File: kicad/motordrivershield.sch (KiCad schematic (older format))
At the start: 40 parts, among them CN1 ARDUINO_MKR, CN2 QWIIC, P1 CONN_01X03, P2 CONN_01X03, U1 PCA9685_TSSOP28, U2 ADS1015

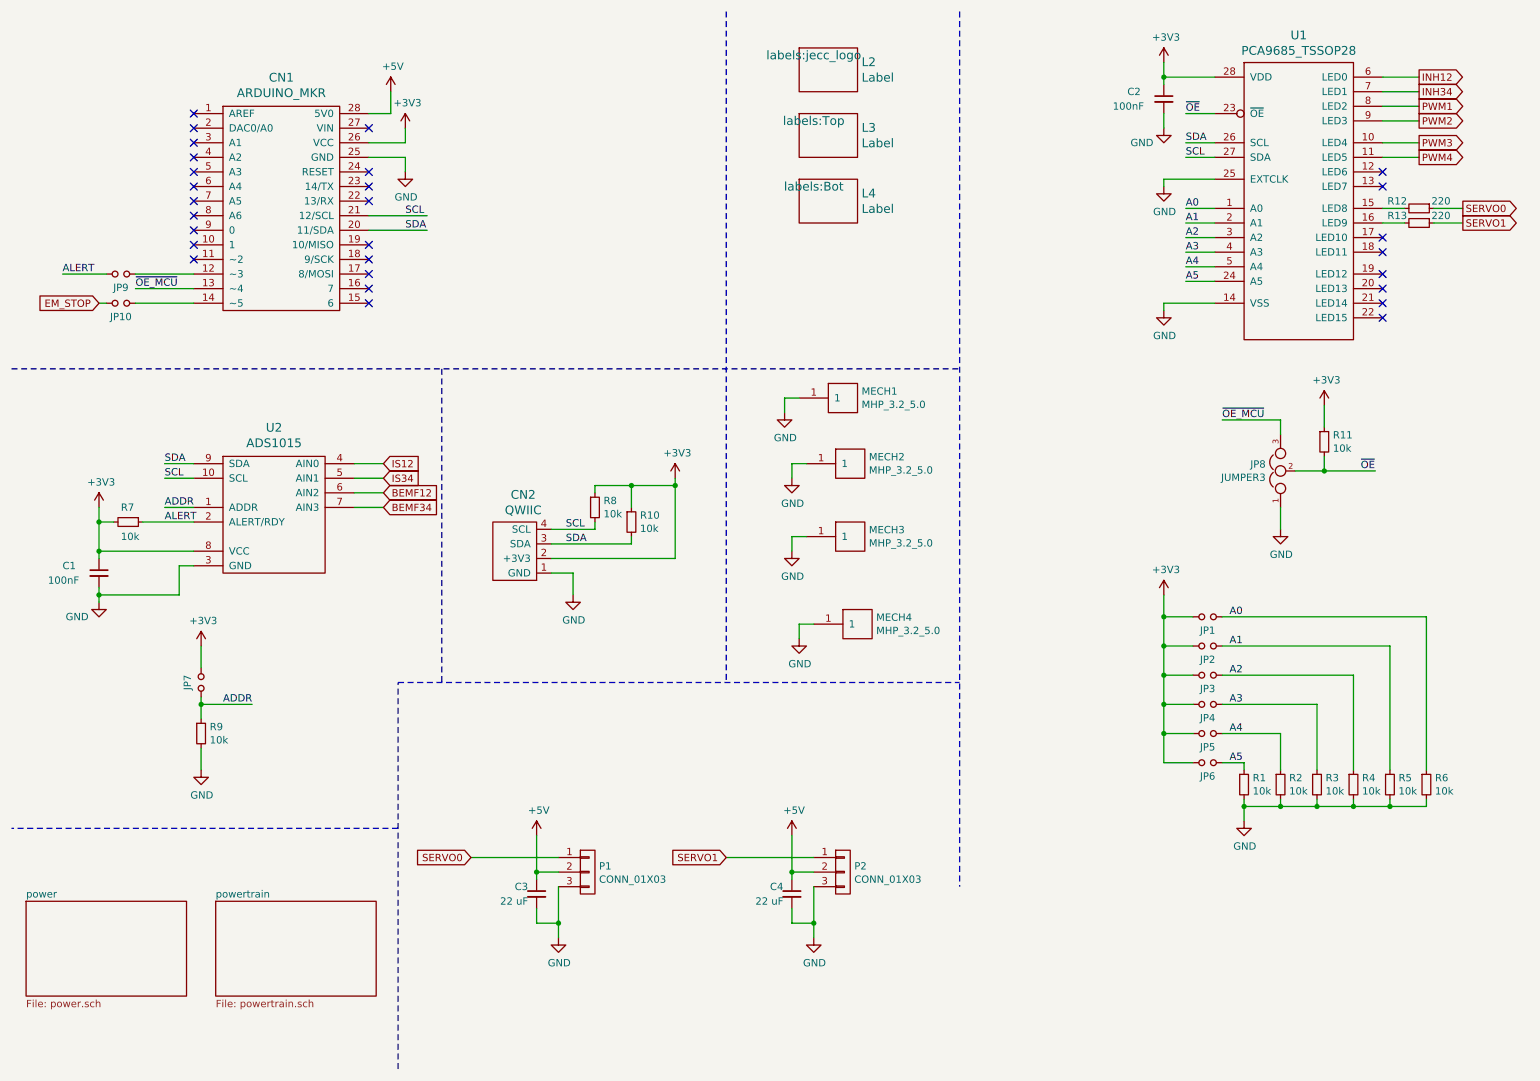
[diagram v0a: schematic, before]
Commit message: added nano footprint
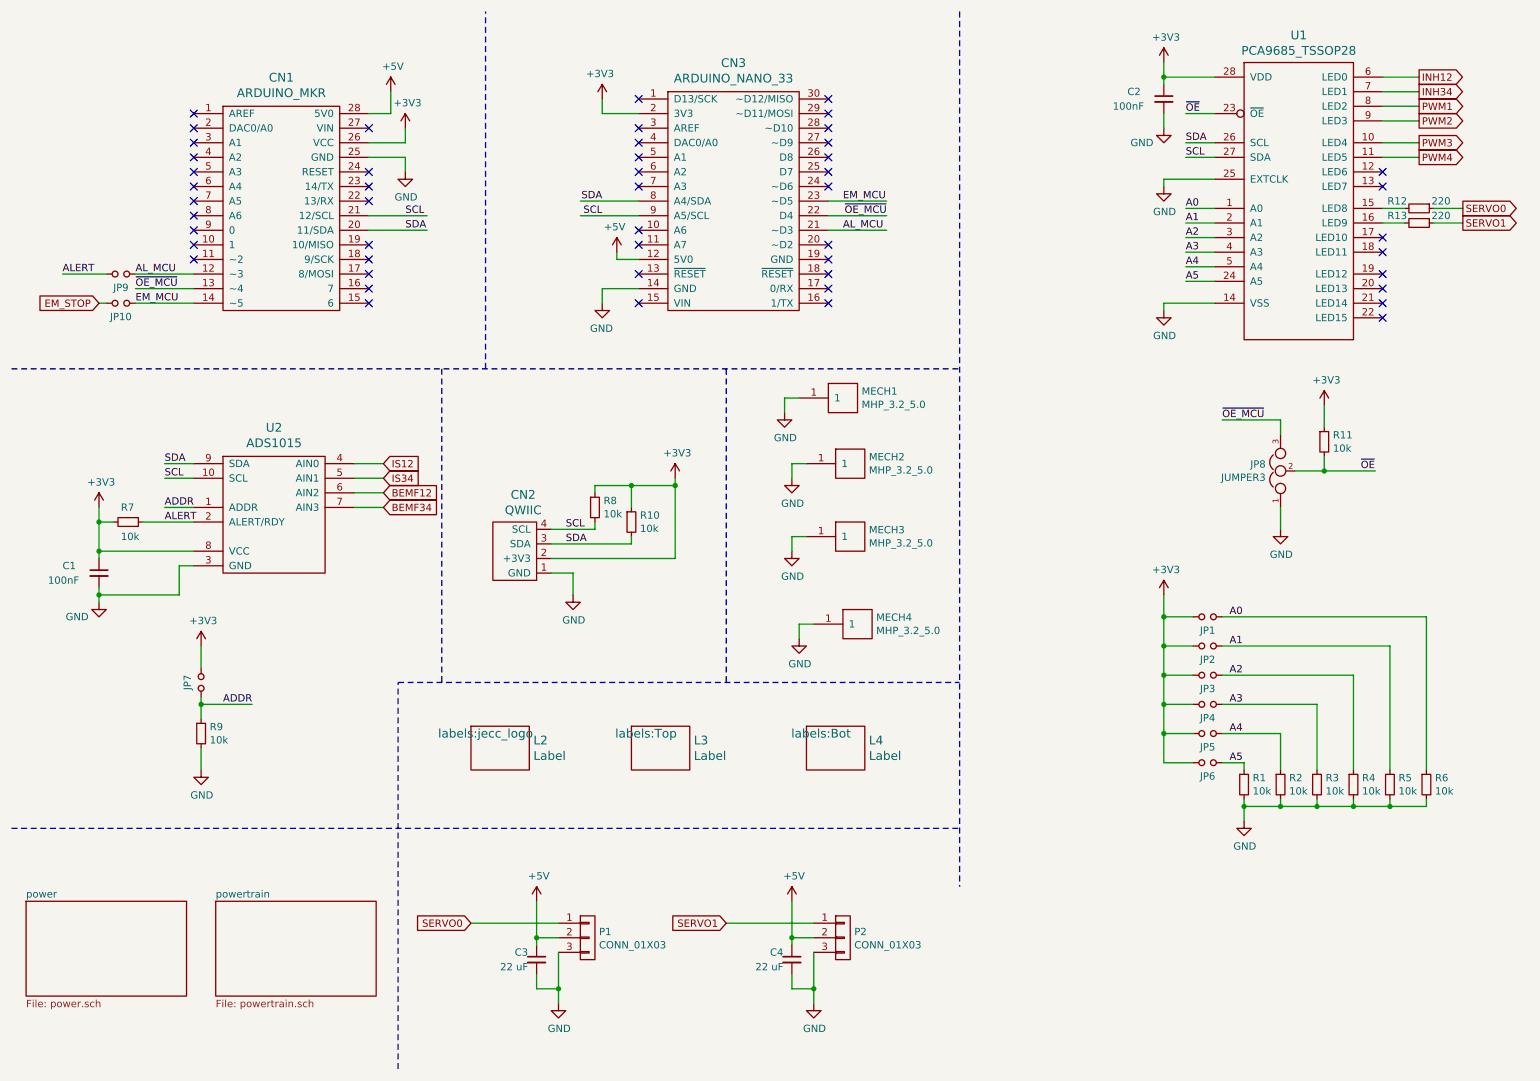
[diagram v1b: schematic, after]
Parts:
- added CN3: ARDUINO_NANO_33, MODULE_compute:ARDUINO_NANO_33, symbol MODULE_compute:ARDUINO_NANO_33
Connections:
- net labels added: AL_MCU, EM_MCU
- wire segments 143 -> 154
- no-connect marks 28 -> 50
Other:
- moved on the sheet: C3, C4, L2, L3, L4, P1, P2

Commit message: changed 5V power rail
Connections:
- wire segments 154 -> 156
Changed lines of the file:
@@
 NoConn ~ 2950 1700
 NoConn ~ 2950 1600
-NoConn ~ 2950 1300
 Wire Wire Line
 	4200 4350 4350 4350
@@
 	1150 2500 1100 2500
 Wire Wire Line
-	2950 1200 3100 1200
-Wire Wire Line
-	3100 1200 3100 1050
+	2950 1300 3100 1300
+Wire Wire Line
+	3100 1300 3100 1150
 $Comp
 L power-supply:+5V #PWR0115
 U 1 1 5F641F07
-P 3100 1050
-F 0 "#PWR0115" H 3100 900 50  0001 C CNN
-F 1 "+5V" H 3115 1223 50  0000 C CNN
-F 2 "" H 3100 1050 50  0000 C CNN
-F 3 "" H 3100 1050 50  0000 C CNN
-	1    3100 1050
+P 3100 1150
+F 0 "#PWR0115" H 3100 1000 50  0001 C CNN
+F 1 "+5V" H 3115 1323 50  0000 C CNN
+F 2 "" H 3100 1150 50  0000 C CNN
+F 3 "" H 3100 1150 50  0000 C CNN
+	1    3100 1150
 	1    0    0    -1
 $EndComp
@@
 Wire Notes Line
 	500  6100 7000 6100
-Wire Wire Line
-	4800 2200 4650 2200
-Wire Wire Line
-	4650 2200 4650 2150
-$Comp
-L power-supply:+5V #PWR0123
-U 1 1 5F68AA89
-P 4650 2150
-F 0 "#PWR0123" H 4650 2000 50  0001 C CNN
-F 1 "+5V" H 4665 2323 50  0000 C CNN
-F 2 "" H 4650 2150 50  0000 C CNN
-F 3 "" H 4650 2150 50  0000 C CNN
-	1    4650 2150
-	-1   0    0    -1
-$EndComp
 Wire Wire Line
 	4800 1200 4550 1200
@@
 	-1   0    0    -1
 $EndComp
-Wire Wire Line
-	4800 2400 4550 2400
 Wire Wire Line
 	4550 2400 4550 2500
@@
 NoConn ~ 6100 2400
 NoConn ~ 6100 2500
-NoConn ~ 4800 2500
 NoConn ~ 4800 2300
 NoConn ~ 4800 2100
@@
 Wire Notes Line
 	3750 2950 3750 500
+Wire Wire Line
+	4800 2400 4550 2400
+$Comp
+L power-supply:+5V #PWR0123
+U 1 1 5F68AA89
+P 4350 2400
+F 0 "#PWR0123" H 4350 2250 50  0001 C CNN
+F 1 "+5V" H 4365 2573 50  0000 C CNN
+F 2 "" H 4350 2400 50  0000 C CNN
+F 3 "" H 4350 2400 50  0000 C CNN
+	1    4350 2400
+	-1   0    0    -1
+$EndComp
+Wire Wire Line
+	4600 2500 4600 2450
+Wire Wire Line
+	4600 2450 4350 2450
+Wire Wire Line
+	4350 2450 4350 2400
+Wire Wire Line
+	4600 2500 4800 2500
+NoConn ~ 2950 1200
+NoConn ~ 4800 2200
 $EndSCHEMATC

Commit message: added leds, updated capacitor values and changed silkscreen
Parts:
- added D5, D6, D7, D8: Led_Small, LEDs:LED_0603, symbol devices:Led_Small
- added R15, R56, R57, R58: 1k, resistors:R_0603, symbol devices:R_0603
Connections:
- wire segments 156 -> 172
- no-connect marks 50 -> 46
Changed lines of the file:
@@
 Wire Wire Line
 	9900 1500 10150 1500
-NoConn ~ 9900 2300
-NoConn ~ 9900 2400
 NoConn ~ 9900 2500
 NoConn ~ 9900 2600
@@
 Wire Notes Line
 	3150 5100 7000 5100
-NoConn ~ 9900 2150
-NoConn ~ 9900 2050
 Wire Wire Line
 	1750 2300 1350 2300
@@
 NoConn ~ 2950 1200
 NoConn ~ 4800 2200
+$Comp
+L devices:R_0603 R15
+U 1 1 5F72B532
+P 10150 2050
+F 0 "R15" V 10100 1900 50  0000 C CNN
+F 1 "1k" V 10100 2200 50  0000 C CNN
+F 2 "resistors:R_0603" H 10150 1900 50  0001 C CNN
+F 3 "" H 10150 2050 50  0000 C CNN
+	1    10150 2050
+	0    1    1    0
+$EndComp
+$Comp
+L devices:R_0603 R56
+U 1 1 5F732F5D
+P 10150 2150
+F 0 "R56" V 10100 2000 50  0000 C CNN
+F 1 "1k" V 10100 2300 50  0000 C CNN
+F 2 "resistors:R_0603" H 10150 2000 50  0001 C CNN
+F 3 "" H 10150 2150 50  0000 C CNN
+	1    10150 2150
+	0    1    1    0
+$EndComp
+$Comp
+L devices:R_0603 R57
+U 1 1 5F73A7B5
+P 10150 2300
+F 0 "R57" V 10100 2150 50  0000 C CNN
+F 1 "1k" V 10100 2450 50  0000 C CNN
+F 2 "resistors:R_0603" H 10150 2150 50  0001 C CNN
+F 3 "" H 10150 2300 50  0000 C CNN
+	1    10150 2300
+	0    1    1    0
+$EndComp
+$Comp
+L devices:R_0603 R58
+U 1 1 5F742075
+P 10150 2400
+F 0 "R58" V 10100 2250 50  0000 C CNN
+F 1 "1k" V 10100 2550 50  0000 C CNN
+F 2 "resistors:R_0603" H 10150 2250 50  0001 C CNN
+F 3 "" H 10150 2400 50  0000 C CNN
+	1    10150 2400
+	0    1    1    0
+$EndComp
+$Comp
+L devices:Led_Small D5
+U 1 1 5F74A32D
+P 10550 2050
+F 0 "D5" H 10700 2000 50  0000 C CNN
+F 1 "Led_Small" H 10100 2000 50  0001 C CNN
+F 2 "LEDs:LED_0603" V 10550 2050 50  0001 C CNN
+F 3 "" V 10550 2050 50  0000 C CNN
+	1    10550 2050
+	-1   0    0    1
+$EndComp
+$Comp
+L devices:Led_Small D6
+U 1 1 5F74C44E
+P 10550 2150
+F 0 "D6" H 10700 2100 50  0000 C CNN
+F 1 "Led_Small" H 10100 2100 50  0001 C CNN
+F 2 "LEDs:LED_0603" V 10550 2150 50  0001 C CNN
+F 3 "" V 10550 2150 50  0000 C CNN
+	1    10550 2150
+	-1   0    0    1
+$EndComp
+$Comp
+L devices:Led_Small D7
+U 1 1 5F753DDF
+P 10550 2300
+F 0 "D7" H 10700 2250 50  0000 C CNN
+F 1 "Led_Small" H 10100 2250 50  0001 C CNN
+F 2 "LEDs:LED_0603" V 10550 2300 50  0001 C CNN
+F 3 "" V 10550 2300 50  0000 C CNN
+	1    10550 2300
+	-1   0    0    1
+$EndComp
+$Comp
+L devices:Led_Small D8
+U 1 1 5F75B602
+P 10550 2400
+F 0 "D8" H 10700 2350 50  0000 C CNN
+F 1 "Led_Small" H 10100 2350 50  0001 C CNN
+F 2 "LEDs:LED_0603" V 10550 2400 50  0001 C CNN
+F 3 "" V 10550 2400 50  0000 C CNN
+	1    10550 2400
+	-1   0    0    1
+$EndComp
+Wire Wire Line
+	9900 2050 10050 2050
+Wire Wire Line
+	9900 2150 10050 2150
+Wire Wire Line
+	9900 2300 10050 2300
+Wire Wire Line
+	9900 2400 10050 2400
+Wire Wire Line
+	10250 2050 10450 2050
+Wire Wire Line
+	10250 2150 10450 2150
+Wire Wire Line
+	10250 2300 10450 2300
+Wire Wire Line
+	10250 2400 10450 2400
+Wire Wire Line
+	10650 2050 10800 2050
+Wire Wire Line
+	10800 2050 10800 2150
+Wire Wire Line
+	10650 2150 10800 2150
+Connection ~ 10800 2150
+Wire Wire Line
+	10800 2150 10800 2300
+Wire Wire Line
+	10650 2300 10800 2300
+Connection ~ 10800 2300
+Wire Wire Line
+	10800 2300 10800 2400
+Wire Wire Line
+	10650 2400 10800 2400
+Connection ~ 10800 2400
+Wire Wire Line
+	10800 2400 10800 2500
+$Comp
+L power-supply:GND #PWR0196
+U 1 1 5F7C6534
+P 10800 2500
+F 0 "#PWR0196" H 10800 2250 50  0001 C CNN
+F 1 "GND" H 10805 2327 50  0000 C CNN
+F 2 "" H 10800 2500 50  0000 C CNN
+F 3 "" H 10800 2500 50  0000 C CNN
+	1    10800 2500
+	1    0    0    -1
+$EndComp
 $EndSCHEMATC

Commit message: bom update
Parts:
- C3, C4: value 22 uF -> 22uF
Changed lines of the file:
@@
 P 4100 7000
 F 0 "C3" H 3950 7050 50  0000 L CNN
-F 1 "22 uF" H 3850 6950 50  0000 L CNN
+F 1 "22uF" H 3850 6950 50  0000 L CNN
 F 2 "capacitors:C_1206" H 4100 6850 50  0001 C CNN
 F 3 "" H 4100 7000 50  0000 C CNN
@@
 P 5850 7000
 F 0 "C4" H 5700 7050 50  0000 L CNN
-F 1 "22 uF" H 5600 6950 50  0000 L CNN
+F 1 "22uF" H 5600 6950 50  0000 L CNN
 F 2 "capacitors:C_1206" H 5850 6850 50  0001 C CNN
 F 3 "" H 5850 7000 50  0000 C CNN

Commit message: swapped sda and scl on pca9685
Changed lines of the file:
@@
 $EndDescr
-$Comp
-L LED-controllers:PCA9685_TSSOP28 U1
-U 1 1 5F5F3EC3
-P 8750 2750
-F 0 "U1" H 9325 4837 60  0000 C CNN
-F 1 "PCA9685_TSSOP28" H 9325 4731 60  0000 C CNN
-F 2 "SSOP:TSSOP-28_4.4x9.7mm_Pitch0.65mm" H 9800 2600 60  0001 C CNN
-F 3 "" H 9350 2700 60  0000 C CNN
-	1    8750 2750
-	1    0    0    -1
-$EndComp
 $Comp
 L devices:Jumper_NO_Small JP1
@@
 	8550 1200 8750 1200
 Wire Wire Line
+	8750 1500 8550 1500
+Wire Wire Line
 	8750 1400 8550 1400
-Wire Wire Line
-	8750 1500 8550 1500
 Text Label 8550 1200 0    50   ~ 0
 ~OE
+Text Label 8550 1500 0    50   ~ 0
+SDA
 Text Label 8550 1400 0    50   ~ 0
-SDA
-Text Label 8550 1500 0    50   ~ 0
 SCL
 Wire Wire Line
@@
 	1    0    0    -1
 $EndComp
+$Comp
+L LED-controllers:PCA9685_TSSOP28 U1
+U 1 1 5FB10F0E
+P 8750 2750
+F 0 "U1" H 9325 4837 60  0000 C CNN
+F 1 "PCA9685_TSSOP28" H 9325 4731 60  0000 C CNN
+F 2 "SSOP:TSSOP-28_4.4x9.7mm_Pitch0.65mm" H 9800 2600 60  0001 C CNN
+F 3 "" H 9350 2700 60  0000 C CNN
+	1    8750 2750
+	1    0    0    -1
+$EndComp

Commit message: blöden servo wegen kompass gemacht
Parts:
- added R14, R55: 0R0, resistors:R_0603, symbol devices:R_0603
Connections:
- net labels added: SERVO0_MCU, SERVO0_PCA, SERVO1_MCU, SERVO1_PCA
- net labels removed: SERVO0, SERVO1
- wire segments 172 -> 186
- no-connect marks 46 -> 42
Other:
- moved on the sheet: C1, C3, C4, P1, P2, R12, R13, R7, U2

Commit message: servos angepasst
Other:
- moved on the sheet: JP10
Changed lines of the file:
@@
 $EndComp
 Wire Wire Line
-	1750 2400 1350 2400
-Wire Wire Line
-	1750 2500 1350 2500
+	1750 1400 1350 1400
+Wire Wire Line
+	1750 1600 1350 1600
 Wire Wire Line
 	2950 2000 3350 2000
 Wire Wire Line
 	2950 1900 3350 1900
-Text Label 1350 2400 0    50   ~ 0
+Text Label 1350 1400 0    50   ~ 0
 ~OE_MCU
-Text GLabel 1100 2500 0    50   Input ~ 0
+Text GLabel 1100 1600 0    50   Input ~ 0
 EM_STOP
 Text Label 3200 1900 0    50   ~ 0
@@
 U 1 1 5F60D737
 P 1250 2300
-F 0 "JP9" H 1250 2393 50  0000 C CNN
+F 0 "JP9" H 1250 2250 50  0000 C CNN
 F 1 "Jumper_NO_Small" H 1260 2240 50  0001 C CNN
 F 2 "wire_pads:SolderJumper_2mm" H 1250 2250 50  0001 C CNN
@@
 L devices:Jumper_NO_Small JP10
 U 1 1 5F61363A
-P 1250 2500
-F 0 "JP10" H 1250 2593 50  0000 C CNN
-F 1 "Jumper_NO_Small" H 1260 2440 50  0001 C CNN
-F 2 "wire_pads:SolderJumper_2mm" H 1250 2450 50  0001 C CNN
-F 3 "" H 1250 2500 50  0000 C CNN
-	1    1250 2500
+P 1250 1600
+F 0 "JP10" H 1250 1693 50  0000 C CNN
+F 1 "Jumper_NO_Small" H 1260 1540 50  0001 C CNN
+F 2 "wire_pads:SolderJumper_2mm" H 1250 1550 50  0001 C CNN
+F 3 "" H 1250 1600 50  0000 C CNN
+	1    1250 1600
 	-1   0    0    1
 $EndComp
@@
 	1150 2300 850  2300
 Wire Wire Line
-	1150 2500 1100 2500
+	1150 1600 1100 1600
 Wire Wire Line
 	2950 1300 3100 1300
@@
 SDA
 Wire Wire Line
-	6100 1900 6500 1900
+	4800 1500 4400 1500
 Wire Wire Line
 	6100 2000 6500 2000
-Text Label 6500 1900 2    50   ~ 0
+Text Label 4400 1500 0    50   ~ 0
 ~OE_MCU
 Wire Wire Line
-	6100 1800 6500 1800
+	4800 1700 4400 1700
 Text Label 1350 2300 0    50   ~ 0
 AL_MCU
-Text Label 1350 2500 0    50   ~ 0
+Text Label 1350 1600 0    50   ~ 0
 EM_MCU
 Text Label 6200 2000 0    50   ~ 0
 AL_MCU
-Text Label 6200 1800 0    50   ~ 0
+Text Label 4700 1700 2    50   ~ 0
 EM_MCU
 NoConn ~ 6100 1100
@@
 Text Label 10250 1950 0    50   ~ 0
 SERVO1_PCA
-Text Label 4200 1500 0    50   ~ 0
+Text Label 6700 1900 2    50   ~ 0
 SERVO0_MCU
 Wire Wire Line
-	4200 1500 4800 1500
-Wire Wire Line
-	4200 1700 4800 1700
-Text Label 4200 1700 0    50   ~ 0
+	6700 1900 6100 1900
+Wire Wire Line
+	6700 1800 6100 1800
+Text Label 6700 1800 2    50   ~ 0
 SERVO1_MCU
-Text Label 1150 1400 0    50   ~ 0
+Text Label 1150 2400 0    50   ~ 0
 SERVO0_MCU
 Wire Wire Line
-	1150 1400 1750 1400
-Wire Wire Line
-	1150 1600 1750 1600
-Text Label 1150 1600 0    50   ~ 0
+	1150 2400 1750 2400
+Wire Wire Line
+	1150 2500 1750 2500
+Text Label 1150 2500 0    50   ~ 0
 SERVO1_MCU
 $Comp

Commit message: blöder servo
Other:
- moved on the sheet: JP10
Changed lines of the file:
@@
 $EndComp
 Wire Wire Line
-	1750 1400 1350 1400
-Wire Wire Line
-	1750 1600 1350 1600
+	1750 2400 1350 2400
+Wire Wire Line
+	1750 2500 1350 2500
 Wire Wire Line
 	2950 2000 3350 2000
 Wire Wire Line
 	2950 1900 3350 1900
-Text Label 1350 1400 0    50   ~ 0
+Text Label 1350 2400 0    50   ~ 0
 ~OE_MCU
-Text GLabel 1100 1600 0    50   Input ~ 0
+Text GLabel 1100 2500 0    50   Input ~ 0
 EM_STOP
 Text Label 3200 1900 0    50   ~ 0
@@
 U 1 1 5F60D737
 P 1250 2300
-F 0 "JP9" H 1250 2250 50  0000 C CNN
+F 0 "JP9" H 1250 2393 50  0000 C CNN
 F 1 "Jumper_NO_Small" H 1260 2240 50  0001 C CNN
 F 2 "wire_pads:SolderJumper_2mm" H 1250 2250 50  0001 C CNN
@@
 L devices:Jumper_NO_Small JP10
 U 1 1 5F61363A
-P 1250 1600
-F 0 "JP10" H 1250 1693 50  0000 C CNN
-F 1 "Jumper_NO_Small" H 1260 1540 50  0001 C CNN
-F 2 "wire_pads:SolderJumper_2mm" H 1250 1550 50  0001 C CNN
-F 3 "" H 1250 1600 50  0000 C CNN
-	1    1250 1600
+P 1250 2500
+F 0 "JP10" H 1250 2593 50  0000 C CNN
+F 1 "Jumper_NO_Small" H 1260 2440 50  0001 C CNN
+F 2 "wire_pads:SolderJumper_2mm" H 1250 2450 50  0001 C CNN
+F 3 "" H 1250 2500 50  0000 C CNN
+	1    1250 2500
 	-1   0    0    1
 $EndComp
@@
 	1150 2300 850  2300
 Wire Wire Line
-	1150 1600 1100 1600
+	1150 2500 1100 2500
 Wire Wire Line
 	2950 1300 3100 1300
@@
 SDA
 Wire Wire Line
-	4800 1500 4400 1500
+	6100 1900 6500 1900
 Wire Wire Line
 	6100 2000 6500 2000
-Text Label 4400 1500 0    50   ~ 0
+Text Label 6500 1900 2    50   ~ 0
 ~OE_MCU
 Wire Wire Line
-	4800 1700 4400 1700
+	6100 1800 6500 1800
 Text Label 1350 2300 0    50   ~ 0
 AL_MCU
-Text Label 1350 1600 0    50   ~ 0
+Text Label 1350 2500 0    50   ~ 0
 EM_MCU
 Text Label 6200 2000 0    50   ~ 0
 AL_MCU
-Text Label 4700 1700 2    50   ~ 0
+Text Label 6200 1800 0    50   ~ 0
 EM_MCU
 NoConn ~ 6100 1100
@@
 Text Label 10250 1950 0    50   ~ 0
 SERVO1_PCA
-Text Label 6700 1900 2    50   ~ 0
+Text Label 4200 1500 0    50   ~ 0
 SERVO0_MCU
 Wire Wire Line
-	6700 1900 6100 1900
-Wire Wire Line
-	6700 1800 6100 1800
-Text Label 6700 1800 2    50   ~ 0
+	4200 1500 4800 1500
+Wire Wire Line
+	4200 1700 4800 1700
+Text Label 4200 1700 0    50   ~ 0
 SERVO1_MCU
-Text Label 1150 2400 0    50   ~ 0
+Text Label 1150 1400 0    50   ~ 0
 SERVO0_MCU
 Wire Wire Line
-	1150 2400 1750 2400
-Wire Wire Line
-	1150 2500 1750 2500
-Text Label 1150 2500 0    50   ~ 0
+	1150 1400 1750 1400
+Wire Wire Line
+	1150 1600 1750 1600
+Text Label 1150 1600 0    50   ~ 0
 SERVO1_MCU
 $Comp
